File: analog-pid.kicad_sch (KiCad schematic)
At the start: 24 parts, among them J1 Conn_01x06_Socket, U1 MCP6004, U2 Opamp_Dual, U3 MCP6004

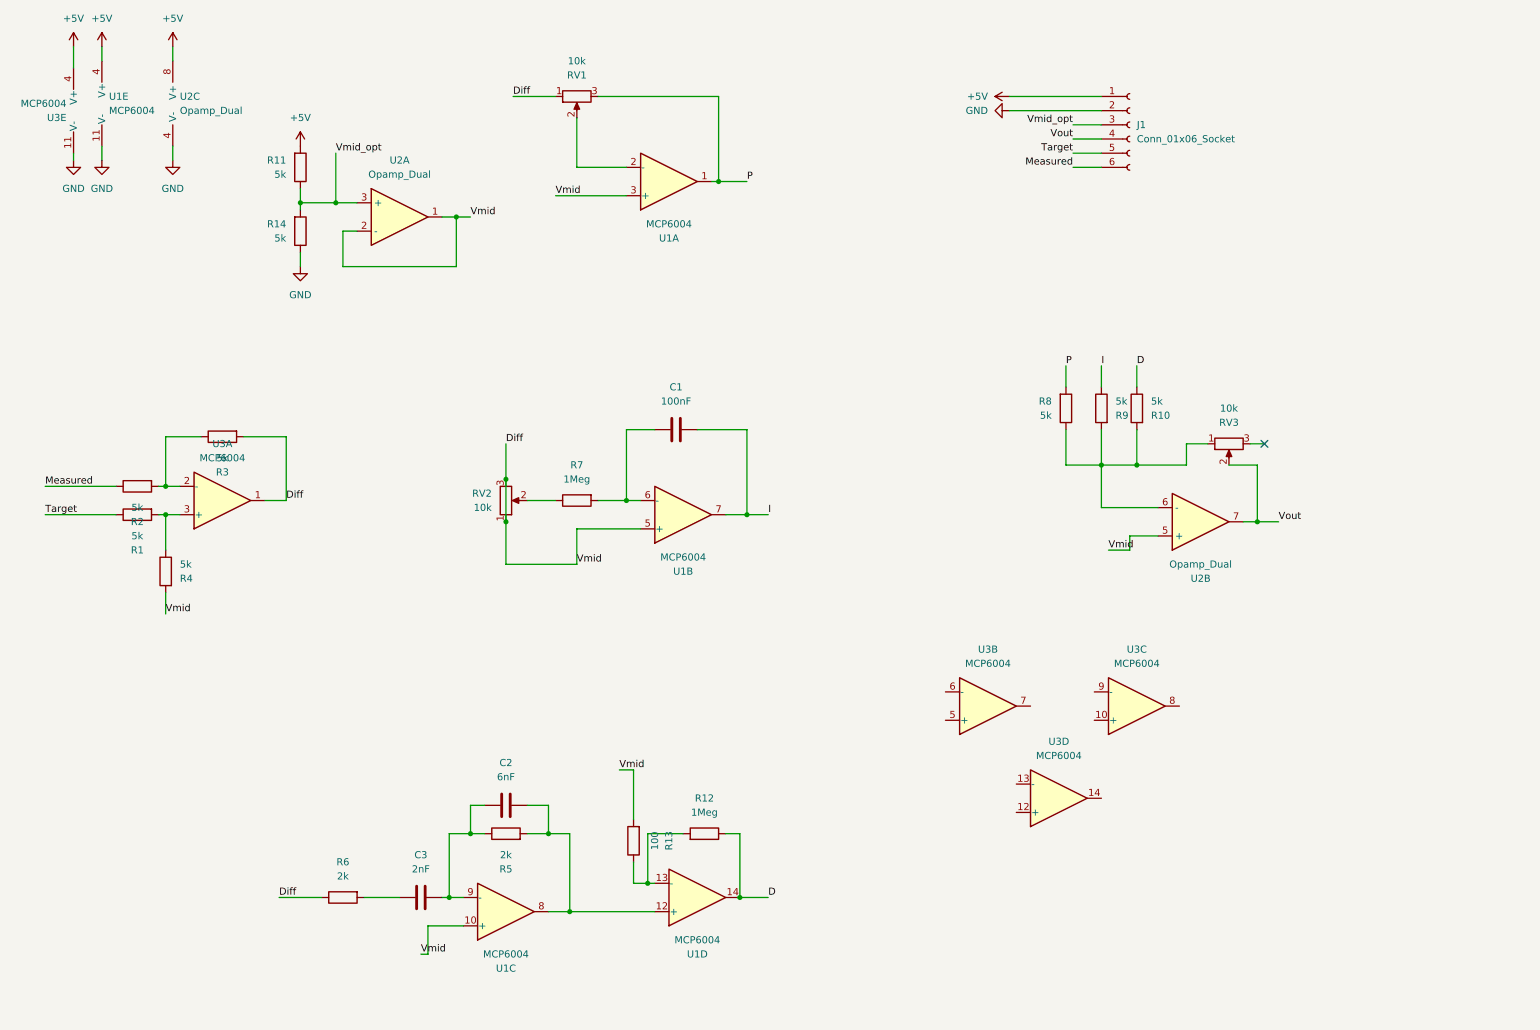
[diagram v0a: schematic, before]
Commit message: anti windup and decoupling caps added
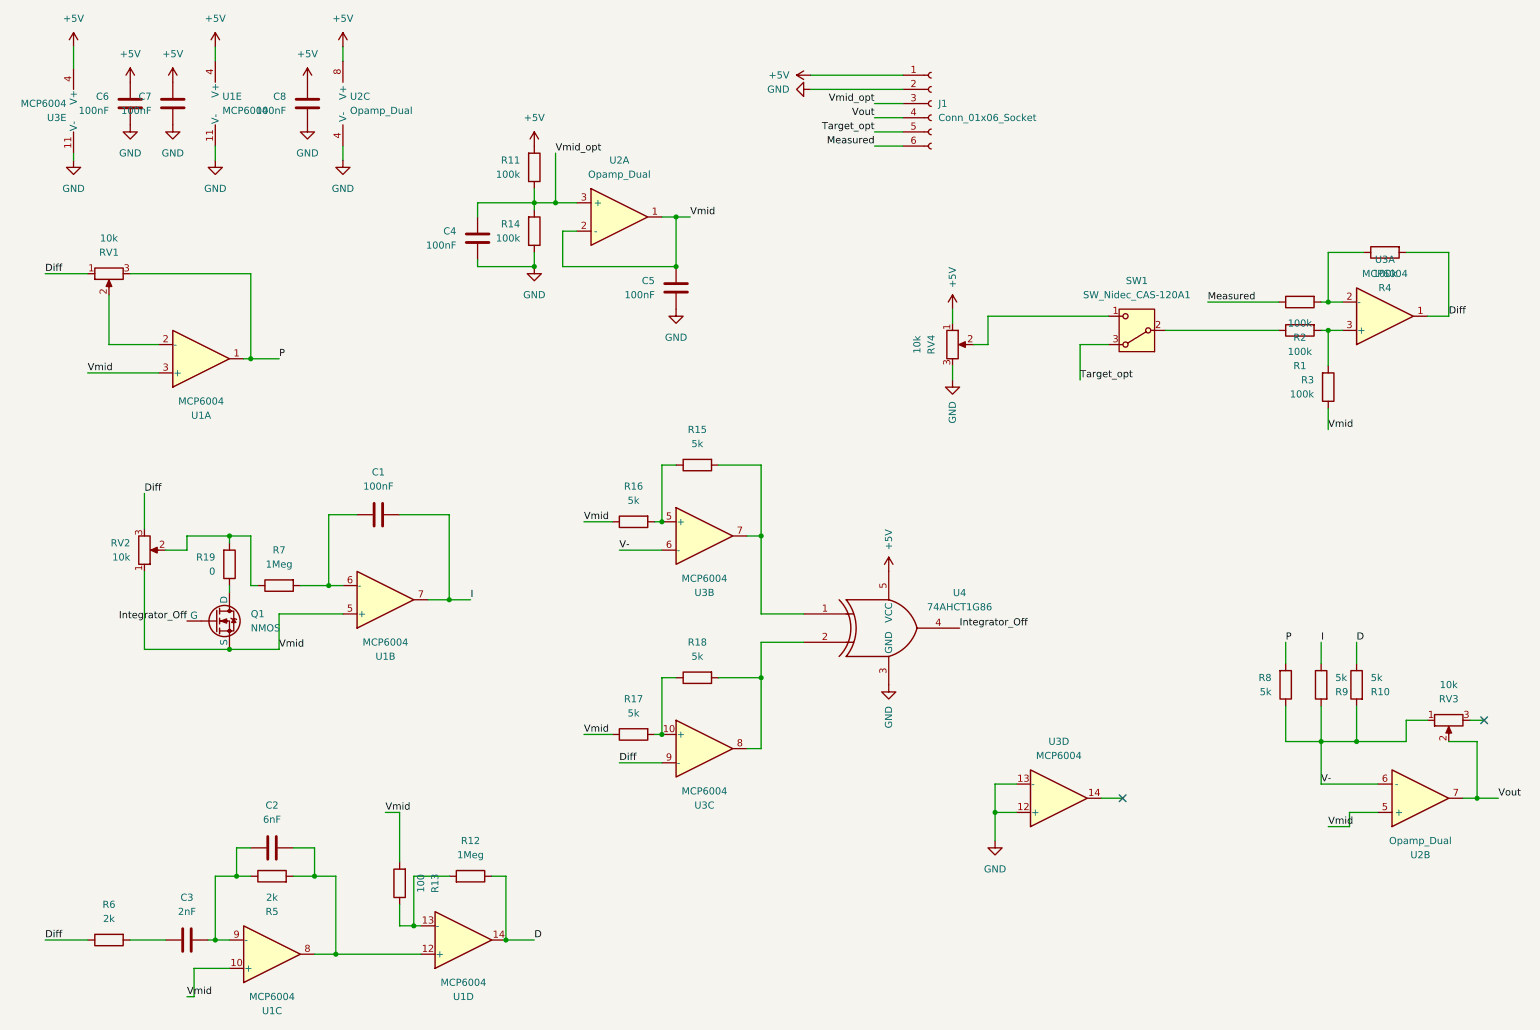
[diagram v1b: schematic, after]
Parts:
- added C4, C5, C6, C7, C8: 100nF, symbol Device:C
- added Q1: NMOS, symbol Simulation_SPICE:NMOS
- added R15, R16, R17, R18: 5k, symbol Device:R
- added R19: 0, symbol Device:R
- added RV4: 10k, symbol Device:R_Potentiometer
- added SW1: SW_Nidec_CAS-120A1, Button_Switch_SMD:Nidec_Copal_CAS-120A, symbol Switch:SW_Nidec_CAS-120A1
- added U4: 74AHCT1G86, symbol 74xGxx:74AHCT1G86
- R1, R11, R14, R2, R3, R4: value 5k -> 100k
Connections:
- net +5V: now also C6.1, C7.1, C8.1, RV4.1, U4.5 (VCC)
- net Diff: now also U3.9 (-); no longer R13.2, R3.2, RV2.1, U1.10 (+), U1.3 (+), U1.5 (+), U2.1, U2.2 (-), U2.5 (+)
- net GND: now also U3.12 (+), U3.13 (-), C4.2, C5.2, C6.2, C7.2, C8.2, RV4.3, U4.3 (GND)
- net Vmid_opt: now also C4.1
- net at R2.2, U3.2 (-): now also R4.1; no longer R3.1
- net V-: now reaches R10.2, R8.1, R9.2, RV3.1, U2.6 (-)
- net V-: now also U3.6 (-)
- net at R7.1, RV2.2: now also R19.2
- net at R1.2, U3.3 (+): now also R3.2; no longer R4.1
- net at U3.5 (+): now also R15.1, R16.2
- net at U3.7: now also R15.2, U4.1
- net at U3.10 (+): now also R17.2, R18.1
- net at U3.8: now also R18.2, U4.2
- net Target: no longer names the net of R1.1
- net Target: now also SW1.2 (B); no longer J1.5 (Pin_5)
- new net: RV4.2, SW1.1 (C)
- new net: Q1.1 (D), R19.1
- new net Integrator_Off: Q1.2 (G), U4.4
- new net Target_opt: J1.5 (Pin_5), SW1.3 (A)
- new net Vmid: C5.1, Q1.3 (S), R13.2, R16.1, R17.1, R3.1, RV2.1, U1.10 (+), U1.3 (+), U1.5 (+), U2.1, U2.2 (-), U2.5 (+)
- no-connect marks 1 -> 2
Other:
- moved on the sheet: C1, C2, C3, J1, R10, R11, R12, R13, R14, R2, R5, R6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

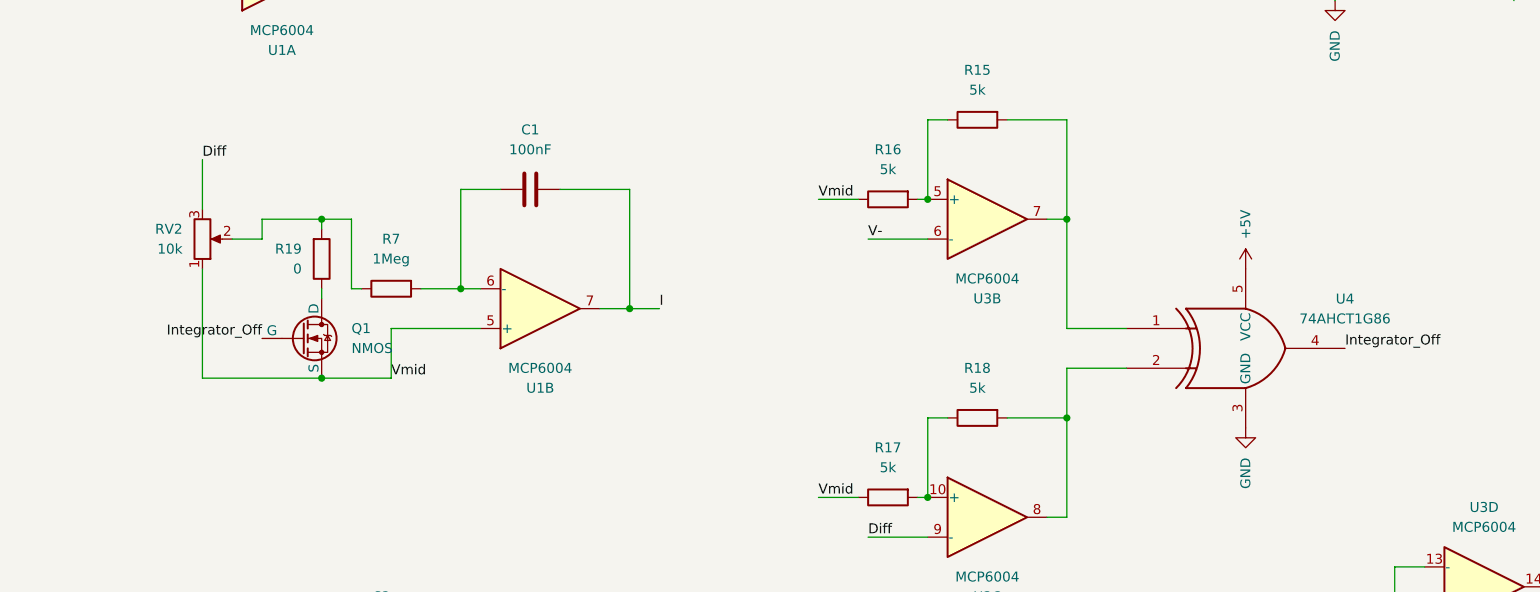
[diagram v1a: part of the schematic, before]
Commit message: Most footprints added
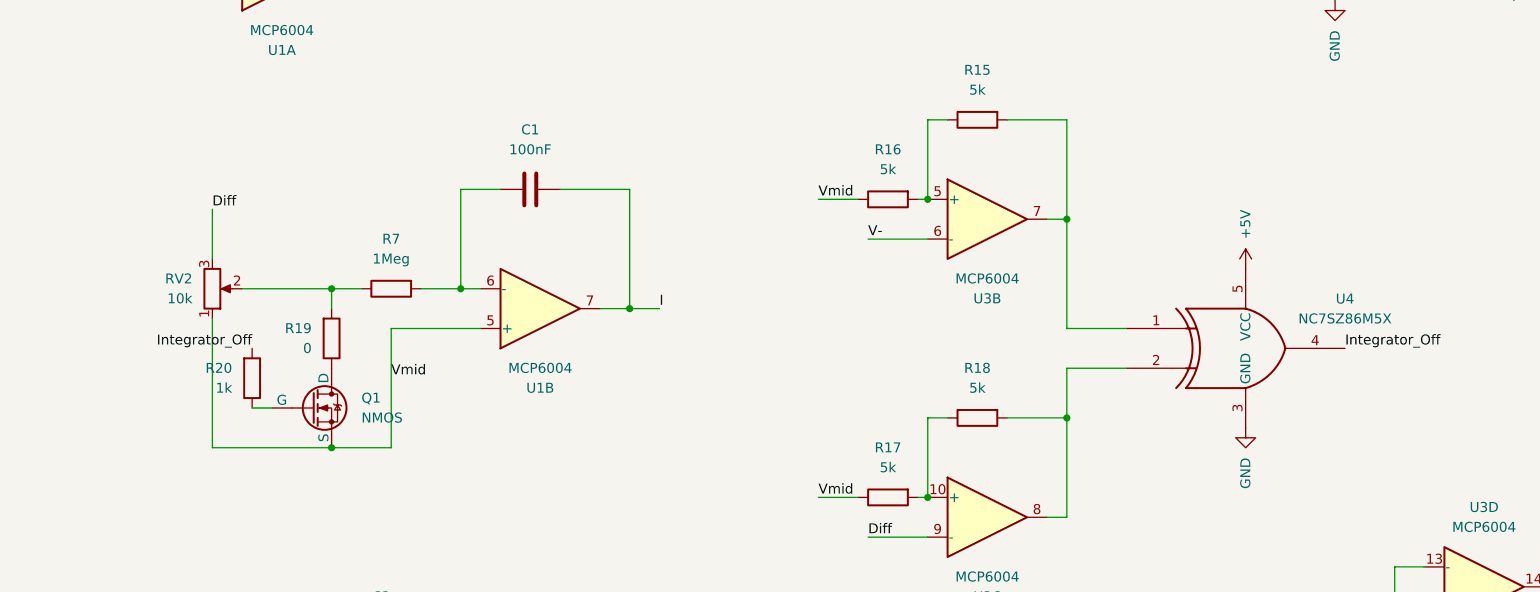
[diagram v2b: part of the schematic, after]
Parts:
- added R20: 1k, Resistor_SMD:R_0805_2012Metric_Pad1.20x1.40mm_HandSolder, symbol Device:R
- C1, C2, C3, C4, C5, C6, C7, C8: footprint (none) -> Capacitor_SMD:C_0805_2012Metric_Pad1.18x1.45mm_HandSolder
- R1, R10, R11, R12, R13, R14, R15, R16, R17, R18, R19, R2, R3, R4, R5, R6, R7, R8, R9: footprint (none) -> Resistor_SMD:R_0805_2012Metric_Pad1.20x1.40mm_HandSolder
- U1: footprint (none) -> Package_DIP:DIP-14_W7.62mm
- U4: value 74AHCT1G86 -> NC7SZ86M5X; footprint (none) -> Package_TO_SOT_SMD:SOT-23-5_HandSoldering
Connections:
- net Integrator_Off: now also R20.2; no longer Q1.2 (G)
- new net: Q1.2 (G), R20.1
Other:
- moved on the sheet: Q1, R19, RV2

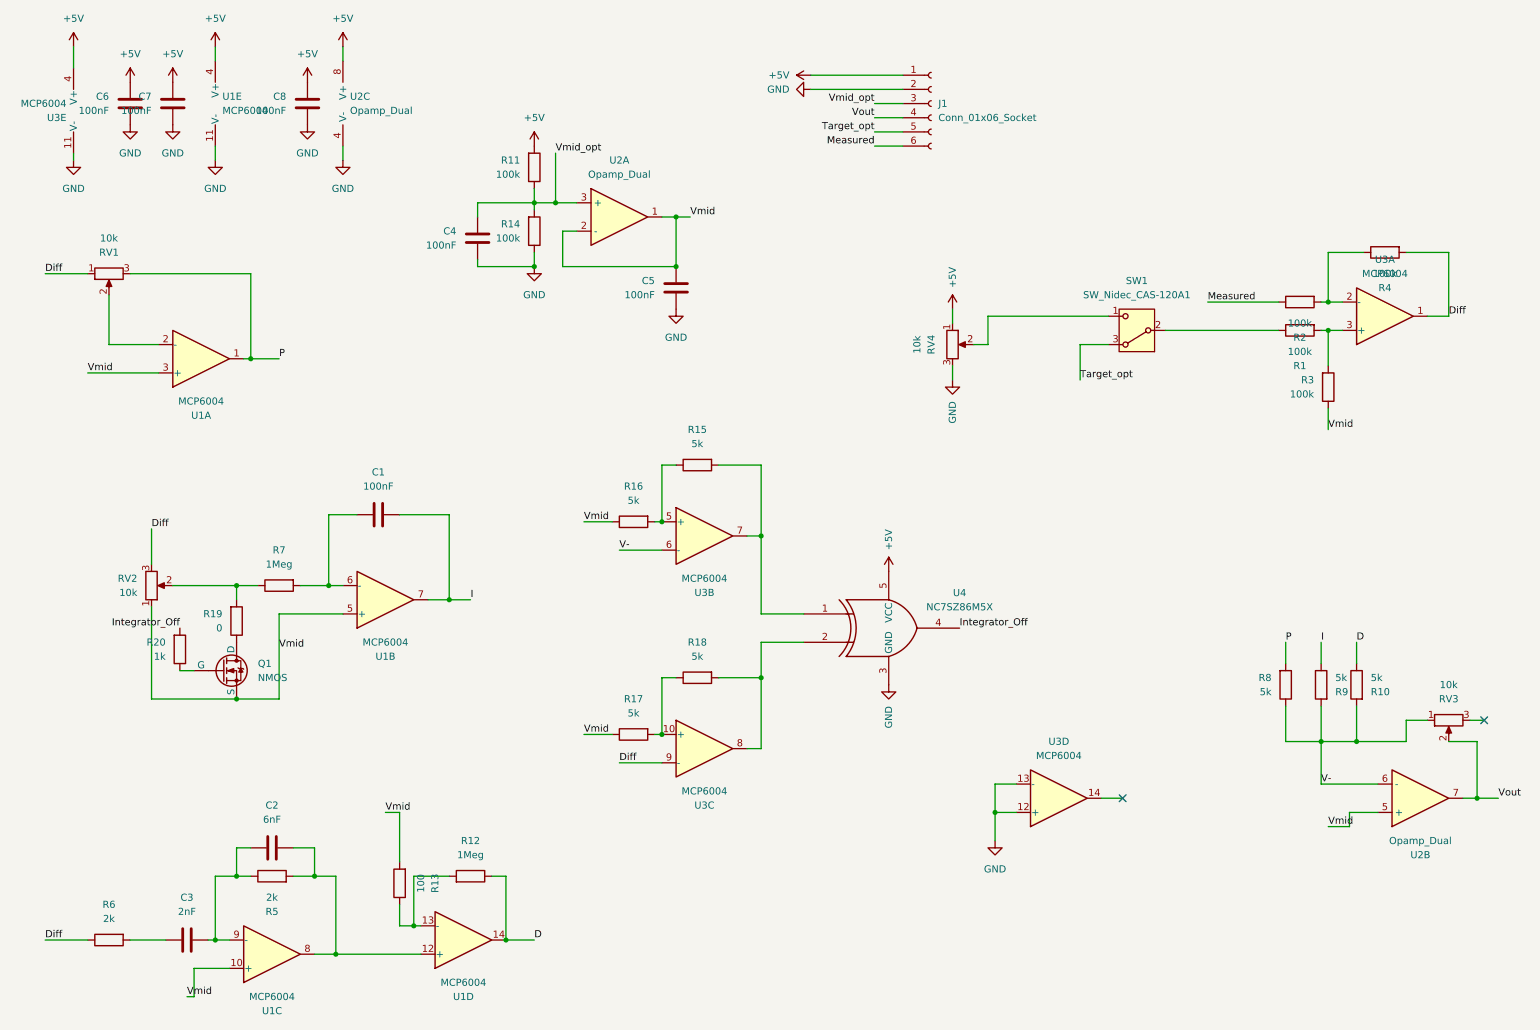
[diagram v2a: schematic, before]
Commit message: schematic + footprints done
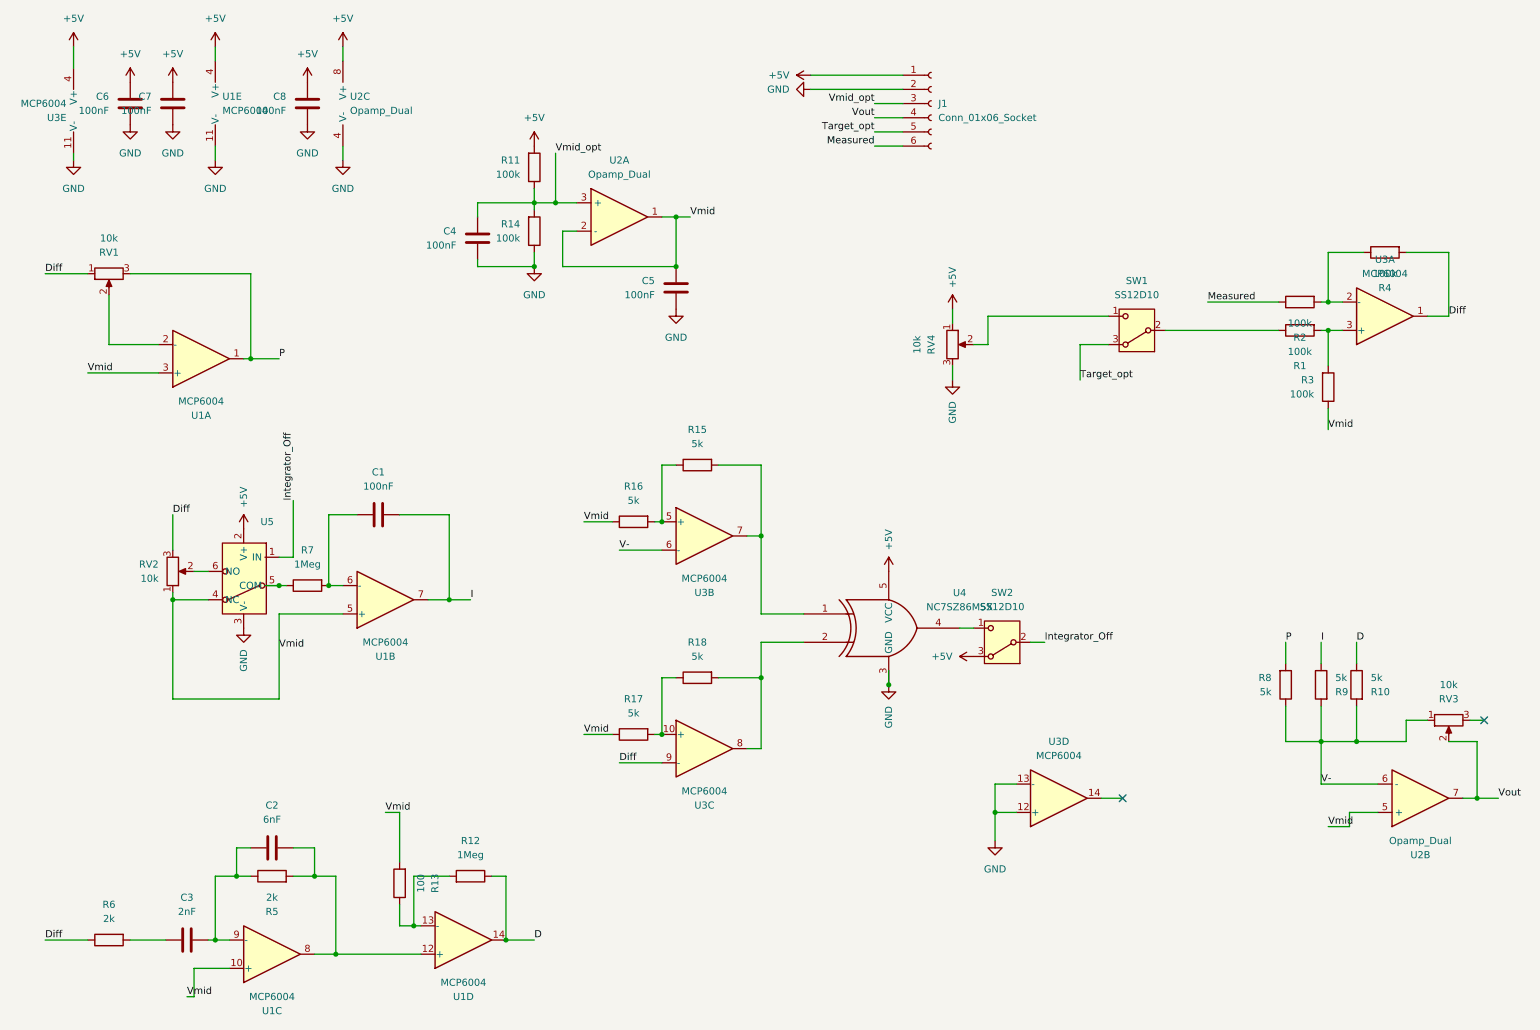
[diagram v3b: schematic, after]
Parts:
- removed Q1: NMOS, symbol Simulation_SPICE:NMOS
- removed R19: 0, Resistor_SMD:R_0805_2012Metric_Pad1.20x1.40mm_HandSolder, symbol Device:R
- removed R20: 1k, Resistor_SMD:R_0805_2012Metric_Pad1.20x1.40mm_HandSolder, symbol Device:R
- added SW2: SS12D10, MyFootprints:SS12D10 SPDT Switch, symbol Switch:SW_Nidec_CAS-120A1
- added U5: ~, Package_TO_SOT_SMD:SOT-363_SC-70-6_Handsoldering, symbol Switch:TS5A4624_SPDT
- J1: footprint (none) -> Connector_PinSocket_2.54mm:PinSocket_1x06_P2.54mm_Vertical
- RV1, RV2, RV3, RV4: footprint (none) -> Potentiometer_THT:Potentiometer_Bourns_3339P_Vertical_HandSoldering
- SW1: value SW_Nidec_CAS-120A1 -> SS12D10; footprint Button_Switch_SMD:Nidec_Copal_CAS-120A -> MyFootprints:SS12D10 SPDT Switch
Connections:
- net +5V: now also SW2.3 (A), U5.2 (V+)
- net GND: now also U5.3 (V-)
- net Integrator_Off: now also SW2.2 (B), U5.1 (IN); no longer U4.4
- net Vmid: now also U5.4 (NC)
- net at RV2.2: now also U5.6 (NO); no longer R7.1
- new net: SW2.1 (C), U4.4
- new net: R7.1, U5.5 (COM)
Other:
- moved on the sheet: R7, RV2
